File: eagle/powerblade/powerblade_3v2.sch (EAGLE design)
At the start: 79 parts, among them J1 JTAG_14PIN_IDC-ND, J2 AC_INF3, J4 TC2030-JLINK-NL, Q1 NTS4173, Q4 2SK1829, U1 TPS62122, U2 MCP6V3, U3 MSP430FR5738, U4 NRF51822QF, U6 MAX9910, U7 OPA2369, X1 16MHz, X3 32.768kHz, Y1 UREACH_XTEND

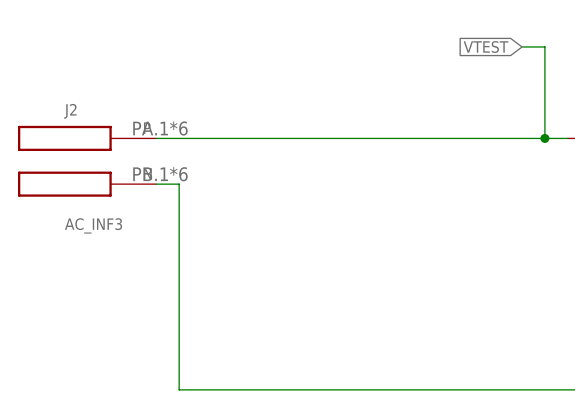
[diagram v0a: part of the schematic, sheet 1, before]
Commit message: disconnected all but A.4 in F3
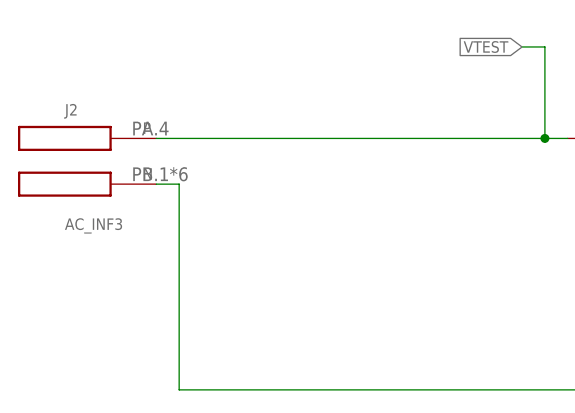
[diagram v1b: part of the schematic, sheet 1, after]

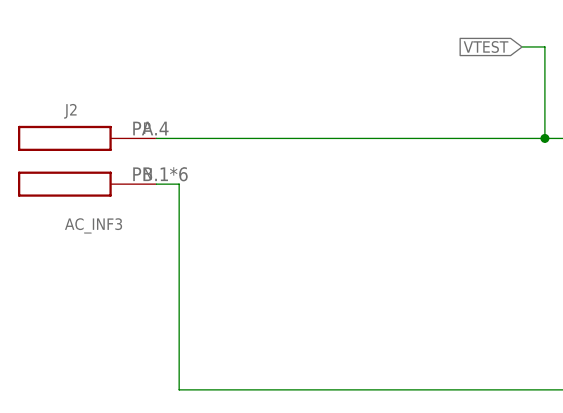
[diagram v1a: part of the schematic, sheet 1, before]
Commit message: more routing on powerblade and moved Phase contact to top (position 3)
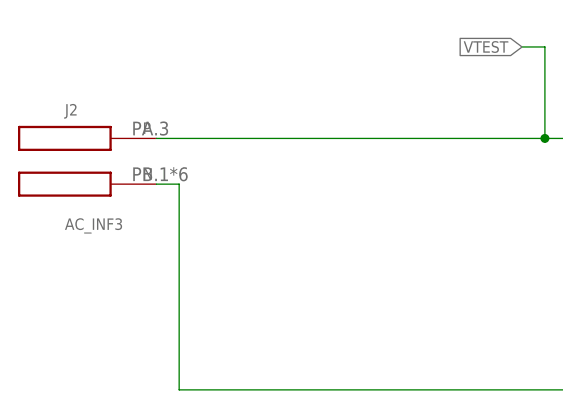
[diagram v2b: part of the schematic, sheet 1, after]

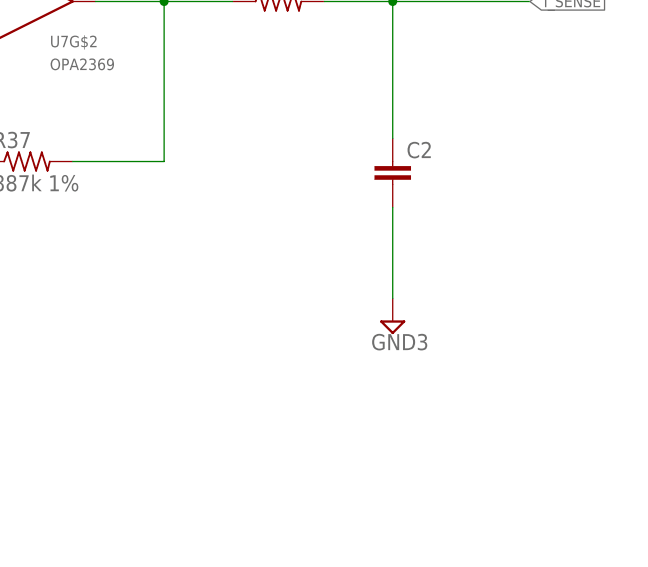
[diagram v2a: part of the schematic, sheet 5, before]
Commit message: switched pins for vfilt and isense
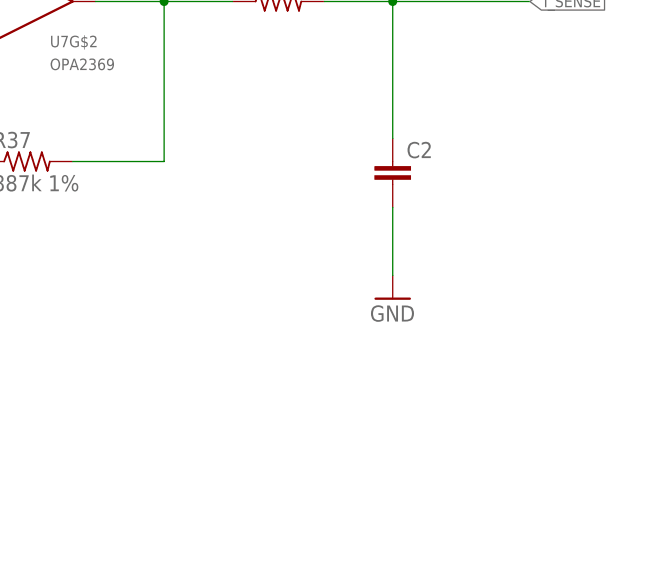
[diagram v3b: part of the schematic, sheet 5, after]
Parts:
- R2, R20, R21, RF, RI1, RI2: device rcl:R-US_R0402_SM -> rcl:R-US_R0402
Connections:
- net GND: now also C2.2
- net GND3: no longer C2.2
- net I_SENSE: now also U3.P1.1/VREF+; no longer U3.P1.0/VREF-
- net VFILT: now also U3.P1.0/VREF-; no longer U3.P1.1/VREF+

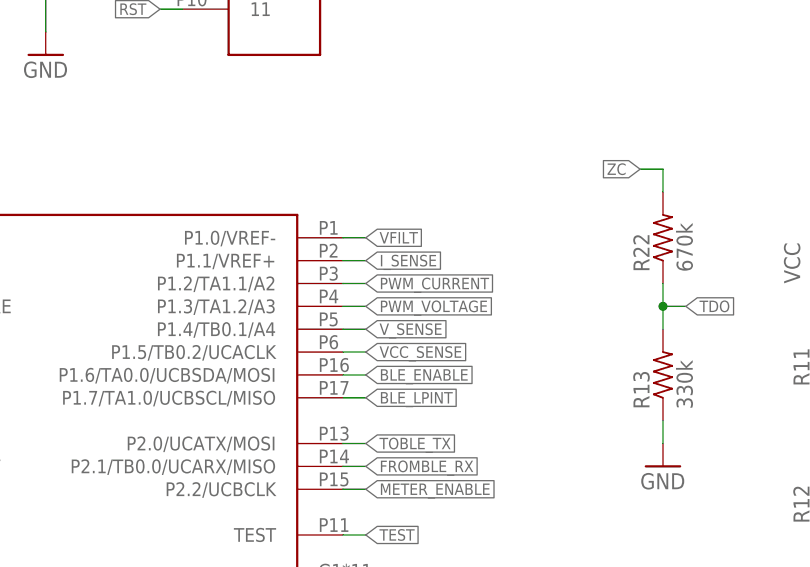
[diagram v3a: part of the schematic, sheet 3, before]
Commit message: more routing in new powerblade
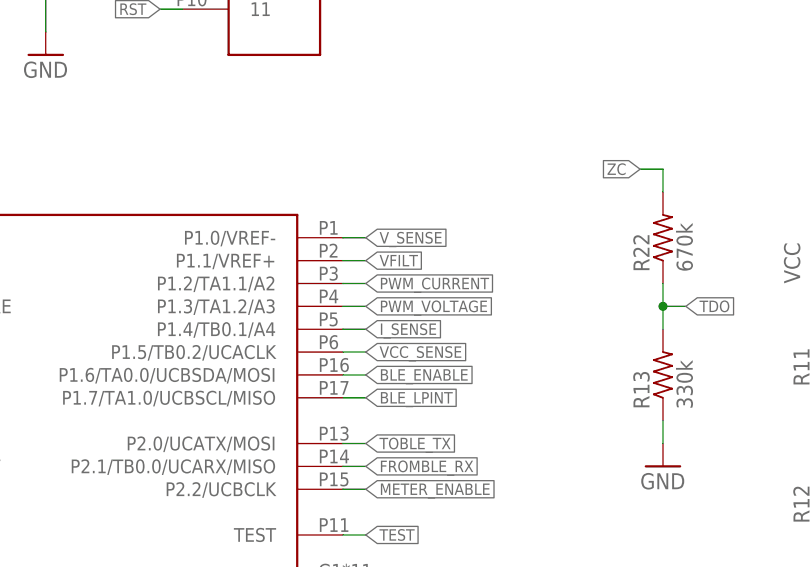
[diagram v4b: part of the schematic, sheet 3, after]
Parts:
- C2: device rcl:C-EUC0402_SM -> rcl:C-EUC0402
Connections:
- net I_SENSE: now also U3.P1.4/TB0.1/A4; no longer U3.P1.1/VREF+
- net VFILT: now also U3.P1.1/VREF+; no longer U3.P1.0/VREF-
- net V_SENSE: now also U3.P1.0/VREF-; no longer U3.P1.4/TB0.1/A4
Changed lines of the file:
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@@
 </part>
 <part name="R2" library="rcl" deviceset="R-US_" device="R0402"/>
-<part name="C2" library="rcl" deviceset="C-EU" device="C0402_SM"/>
+<part name="C2" library="rcl" deviceset="C-EU" device="C0402"/>
 <part name="U2" library="powerfilm" deviceset="MCP6V3" device="">
 <attribute name="DIGIKEY_POP" value="296-19547-1-ND"/>
@@
 <net name="V_SENSE" class="0">
 <segment>
+<label x="27.94" y="17.78" size="1.27" layer="95" xref="yes"/>
+<pinref part="U3" gate="G$1" pin="P1.0/VREF-"/>
+<wire x1="25.4" y1="17.78" x2="27.94" y2="17.78" width="0.1524" layer="91"/>
+</segment>
+</net>
+<net name="I_SENSE" class="0">
+<segment>
+<label x="27.94" y="7.62" size="1.27" layer="95" xref="yes"/>
 <pinref part="U3" gate="G$1" pin="P1.4/TB0.1/A4"/>
-<wire x1="27.94" y1="7.62" x2="25.4" y2="7.62" width="0.1524" layer="91"/>
-<label x="27.94" y="7.62" size="1.27" layer="95" xref="yes"/>
-</segment>
-</net>
-<net name="I_SENSE" class="0">
-<segment>
-<label x="27.94" y="15.24" size="1.27" layer="95" xref="yes"/>
-<pinref part="U3" gate="G$1" pin="P1.1/VREF+"/>
-<wire x1="25.4" y1="15.24" x2="27.94" y2="15.24" width="0.1524" layer="91"/>
+<wire x1="25.4" y1="7.62" x2="27.94" y2="7.62" width="0.1524" layer="91"/>
 </segment>
 </net>
@@
 <net name="VFILT" class="0">
 <segment>
-<label x="27.94" y="17.78" size="1.27" layer="95" xref="yes"/>
-<pinref part="U3" gate="G$1" pin="P1.0/VREF-"/>
-<wire x1="25.4" y1="17.78" x2="27.94" y2="17.78" width="0.1524" layer="91"/>
-</segment>
-</net>
+<label x="27.94" y="15.24" size="1.27" layer="95" xref="yes"/>
+<pinref part="U3" gate="G$1" pin="P1.1/VREF+"/>
+<wire x1="25.4" y1="15.24" x2="27.94" y2="15.24" width="0.1524" layer="91"/>
+</segment>
+</net>

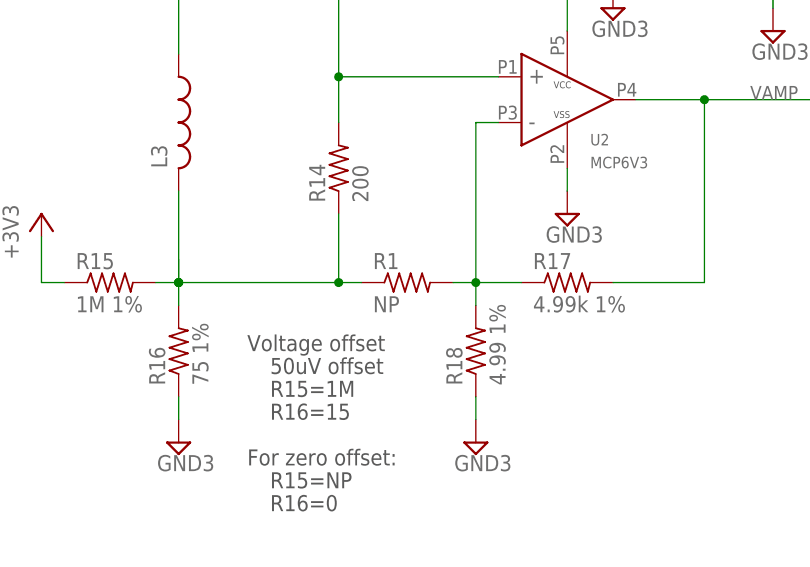
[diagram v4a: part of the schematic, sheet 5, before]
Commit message: more routing and fixed errors
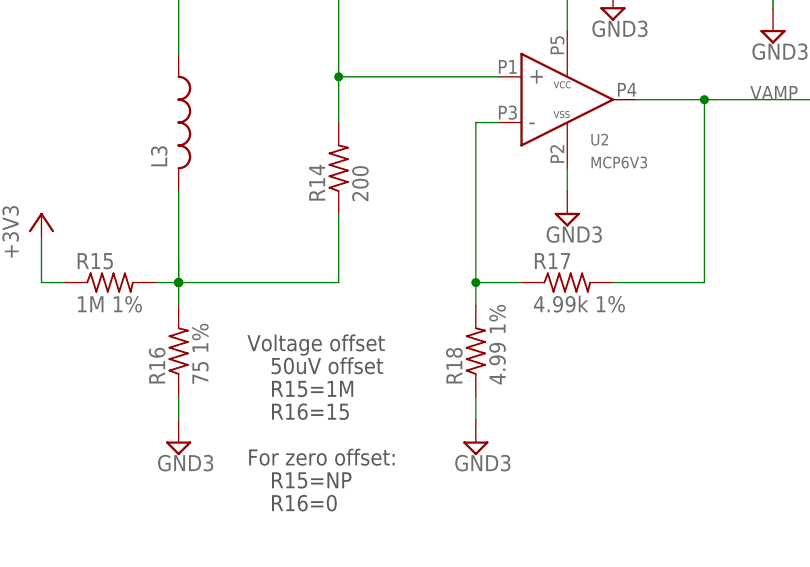
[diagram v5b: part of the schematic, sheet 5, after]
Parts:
- removed R1: NP, rcl:R-US_R0402_SM
- R2, R21: device rcl:R-US_R0402 -> rcl:R-US_R0402_SM
- R6, R7: device rcl:R-US_R0402_SM -> rcl:R-US_R0402
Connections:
- net N$37: no longer R1.1
- net N$65: no longer R1.2
- net VFILT: no longer U3.P1.1/VREF+
- net V_SENSE: now also U3.P1.1/VREF+; no longer U3.P1.0/VREF-
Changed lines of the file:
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@@
 <attribute name="DIGIKEY" value="490-4990-1-ND"/>
 </part>
-<part name="R7" library="rcl" deviceset="R-US_" device="R0402_SM" value="560k">
+<part name="R7" library="rcl" deviceset="R-US_" device="R0402" value="560k">
 <attribute name="DIGIKEY" value="P560KLCT-ND"/>
 </part>
@@
 <attribute name="DIGIKEY" value="P1.00MLCT-ND"/>
 </part>
-<part name="R21" library="rcl" deviceset="R-US_" device="R0402" value="1M 1%">
+<part name="R21" library="rcl" deviceset="R-US_" device="R0402_SM" value="1M 1%">
 <attribute name="DIGIKEY" value="P1.00MLCT-ND"/>
 </part>
@@
 <attribute name="DIGIKEY" value="P16.0KLCT-ND"/>
 </part>
-<part name="R2" library="rcl" deviceset="R-US_" device="R0402"/>
+<part name="R2" library="rcl" deviceset="R-US_" device="R0402_SM"/>
 <part name="C2" library="rcl" deviceset="C-EU" device="C0402"/>
 <part name="U2" library="powerfilm" deviceset="MCP6V3" device="">
@@
 <part name="Q4" library="powerfilm" deviceset="2SK1829" device=""/>
 <part name="SUPPLY19" library="supply2" deviceset="GND3" device=""/>
-<part name="R6" library="rcl" deviceset="R-US_" device="R0402_SM" value="660k">
+<part name="R6" library="rcl" deviceset="R-US_" device="R0402" value="660k">
 <attribute name="DIGIKEY" value="P665KLCT-ND"/>
 </part>
@@
 </part>
 <part name="Y1" library="powerfilm" deviceset="UREACH_XTEND" device=""/>
-<part name="R1" library="rcl" deviceset="R-US_" device="R0402_SM" value="NP">
-<attribute name="DIGIKEY" value="NP"/>
-<attribute name="DIGIKEY_2" value="P0.0JCT-ND"/>
-</part>
 <part name="C24" library="rcl" deviceset="C-EU" device="C0402_SM" value="0.1uF">
 <attribute name="DIGIKEY" value="445-4952-1-ND"/>
@@
 <net name="V_SENSE" class="0">
 <segment>
-<label x="27.94" y="17.78" size="1.27" layer="95" xref="yes"/>
-<pinref part="U3" gate="G$1" pin="P1.0/VREF-"/>
-<wire x1="25.4" y1="17.78" x2="27.94" y2="17.78" width="0.1524" layer="91"/>
+<label x="27.94" y="15.24" size="1.27" layer="95" xref="yes"/>
+<pinref part="U3" gate="G$1" pin="P1.1/VREF+"/>
+<wire x1="25.4" y1="15.24" x2="27.94" y2="15.24" width="0.1524" layer="91"/>
 </segment>
 </net>
@@
 <wire x1="27.94" y1="10.16" x2="25.4" y2="10.16" width="0.1524" layer="91"/>
 <label x="27.94" y="10.16" size="1.27" layer="95" xref="yes"/>
-</segment>
-</net>
-<net name="VFILT" class="0">
-<segment>
-<label x="27.94" y="15.24" size="1.27" layer="95" xref="yes"/>
-<pinref part="U3" gate="G$1" pin="P1.1/VREF+"/>
-<wire x1="25.4" y1="15.24" x2="27.94" y2="15.24" width="0.1524" layer="91"/>
 </segment>
 </net>
@@
 <instance part="SUPPLY28" gate="G$1" x="116.84" y="-2.54"/>
 <instance part="GND2" gate="1" x="20.32" y="-88.9"/>
-<instance part="R1" gate="G$1" x="76.2" y="-30.48">
-<attribute name="DIGIKEY" x="76.2" y="-30.48" size="1.27" layer="96" display="off"/>
-<attribute name="DIGIKEY_2" x="76.2" y="-30.48" size="1.27" layer="96" display="off"/>
-</instance>
 <instance part="C13" gate="G$1" x="-20.32" y="5.08" smashed="yes">
 <attribute name="DIGIKEY" x="-20.32" y="5.08" size="1.778" layer="96" display="off"/>
@@
 <pinref part="L3" gate="G$1" pin="2"/>
 <wire x1="50.8" y1="-20.32" x2="50.8" y2="-30.48" width="0.1524" layer="91"/>
-<pinref part="R1" gate="G$1" pin="1"/>
-<wire x1="71.12" y1="-30.48" x2="68.58" y2="-30.48" width="0.1524" layer="91"/>
-<junction x="68.58" y="-30.48"/>
 </segment>
 </net>
@@
 <junction x="83.82" y="-30.48"/>
 <pinref part="U2" gate="G$1" pin="IN-"/>
-<pinref part="R1" gate="G$1" pin="2"/>
-<wire x1="81.28" y1="-30.48" x2="83.82" y2="-30.48" width="0.1524" layer="91"/>
-</segment>
-</net>
+</segment>
+</net>

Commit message: more routing in powerblade
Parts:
- R11, R12, R13, R22, R9: device rcl:R-US_R0402_SM -> rcl:R-US_R0402
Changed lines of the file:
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@@
 <attribute name="DIGIKEY" value="P560KLCT-ND"/>
 </part>
-<part name="R9" library="rcl" deviceset="R-US_" device="R0402_SM" value="180k">
+<part name="R9" library="rcl" deviceset="R-US_" device="R0402" value="180k">
 <attribute name="DIGIKEY" value="P180KLCT-ND"/>
 </part>
@@
 <part name="+3V7" library="supply1" deviceset="+3V3" device=""/>
 <part name="GND23" library="supply1" deviceset="GND" device=""/>
-<part name="R11" library="rcl" deviceset="R-US_" device="R0402_SM" value="670k">
+<part name="R11" library="rcl" deviceset="R-US_" device="R0402" value="670k">
 <attribute name="DIGIKEY" value="P665KLCT-ND"/>
 </part>
-<part name="R12" library="rcl" deviceset="R-US_" device="R0402_SM" value="330k">
+<part name="R12" library="rcl" deviceset="R-US_" device="R0402" value="330k">
 <attribute name="DIGIKEY" value="P330KLCT-ND"/>
 </part>
@@
 <part name="SUPPLY28" library="supply2" deviceset="GND3" device=""/>
 <part name="GND2" library="supply1" deviceset="GND" device=""/>
-<part name="R13" library="rcl" deviceset="R-US_" device="R0402_SM" value="330k">
+<part name="R13" library="rcl" deviceset="R-US_" device="R0402" value="330k">
 <attribute name="DIGIKEY" value="P330KLCT-ND"/>
 </part>
-<part name="R22" library="rcl" deviceset="R-US_" device="R0402_SM" value="670k">
+<part name="R22" library="rcl" deviceset="R-US_" device="R0402" value="670k">
 <attribute name="DIGIKEY" value="P665KLCT-ND"/>
 </part>
